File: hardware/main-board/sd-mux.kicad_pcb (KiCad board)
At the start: 2 copper layers, 75.4 x 114 mm, 91 parts, among them J1 USDCARD, P1 USB_OTG, P10 BARREL_JACK, P2 61400416021, P3 61400416021, P4 CONN_01X06, P5 BARREL_JACK, P6 IDC_02X04, P7 IDC_02X04, P8 USB_OTG, P9 USB_A, Q1 IRF7606PBF, Q2 IRF7606PBF, Q3 IRF7606PBF, Q4 IRF7606PBF, Q5 2N7002, Q6 2N7002, Q7 IRF7606PBF, Q8 IRF7606PBF, U1 TS3USB30EDGSR, U2 FT245RL, U3 TUSB4041IPAPR, U4 74AHC1G14, U5 TLV73333, U6 TLV73311, U7 74AHC1G14, U8 TS3A27518E, Y1 24MHz

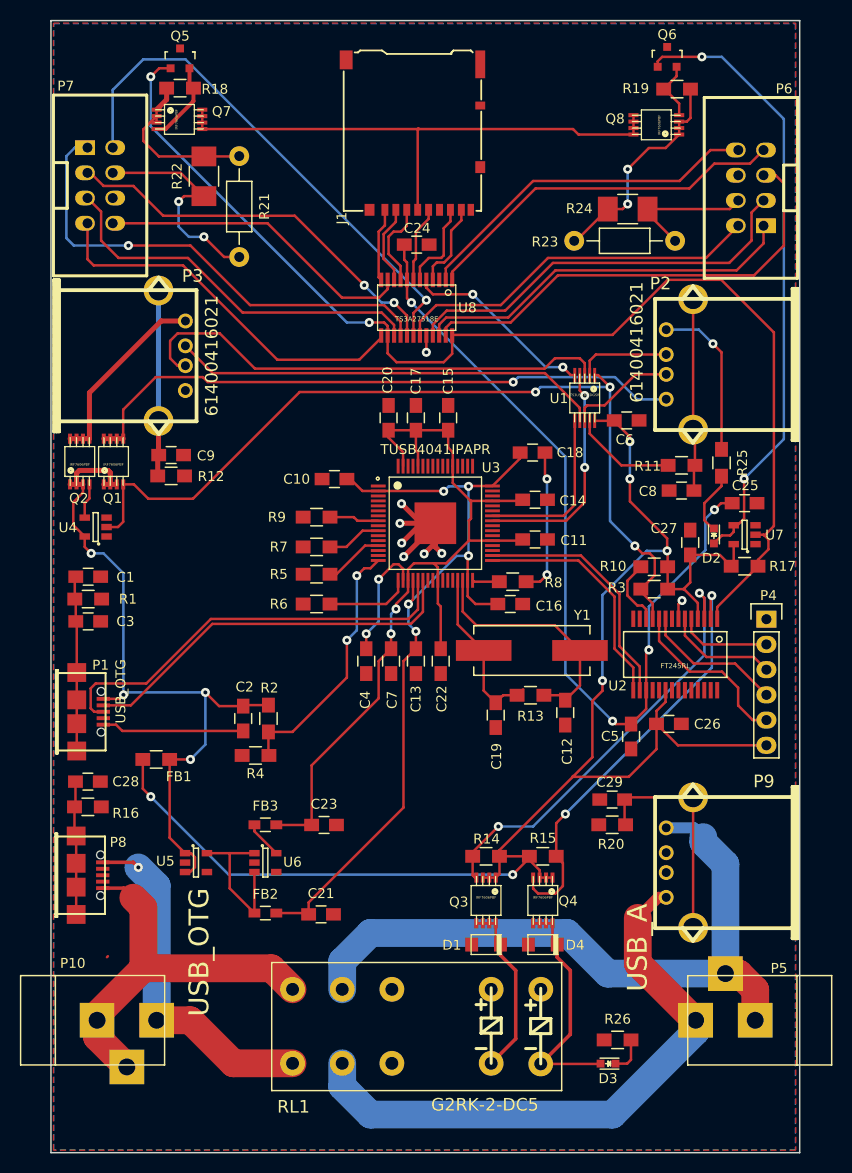
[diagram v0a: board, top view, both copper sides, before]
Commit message: Update BOM and layout labels
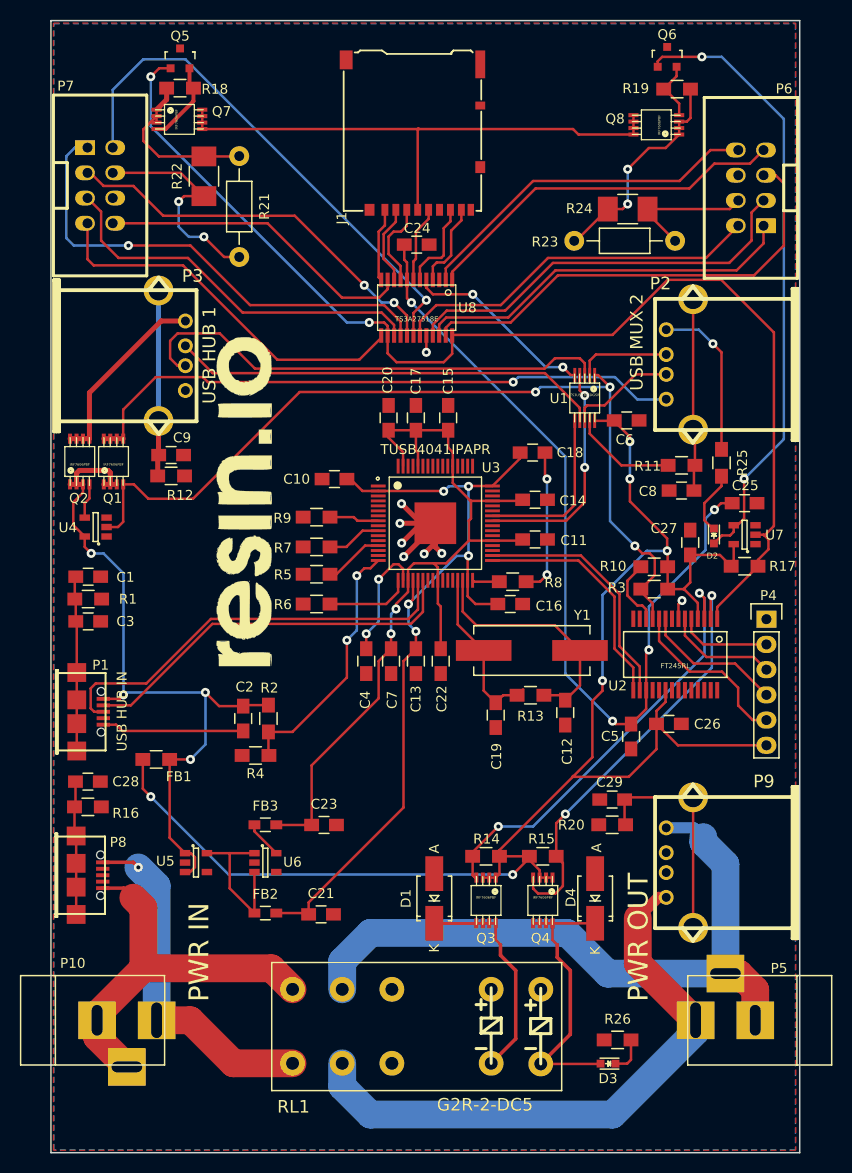
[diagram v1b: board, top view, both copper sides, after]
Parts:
- added G***: LOGO, footprints:logo, F.Cu at (137.7, 82.0)
- D1, D4: value ES1AL -> ES1A-LTP; footprint footprints:do219ab -> Diodes_SMD:SMA_Handsoldering
- P1: value USB_OTG -> USB HUB IN
- P2: value 61400416021 -> USB MUX 2
- P3: value 61400416021 -> USB HUB 1
- P8: value USB_OTG -> PWR IN
- P9: value USB_A -> PWR OUT
- RL1: value G2RK-2-DC5 -> G2R-2-DC5
- moved D4 7.03 mm to (173.0, 122.0), turned to 90 degrees
- moved D1 6.98 mm to (156.8, 122.0), turned to 90 degrees
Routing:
- net Net-(D1-Pad1): track 17.9 -> 26.2 mm
- net Net-(D3-Pad2): track 24.2 -> 28.5 mm

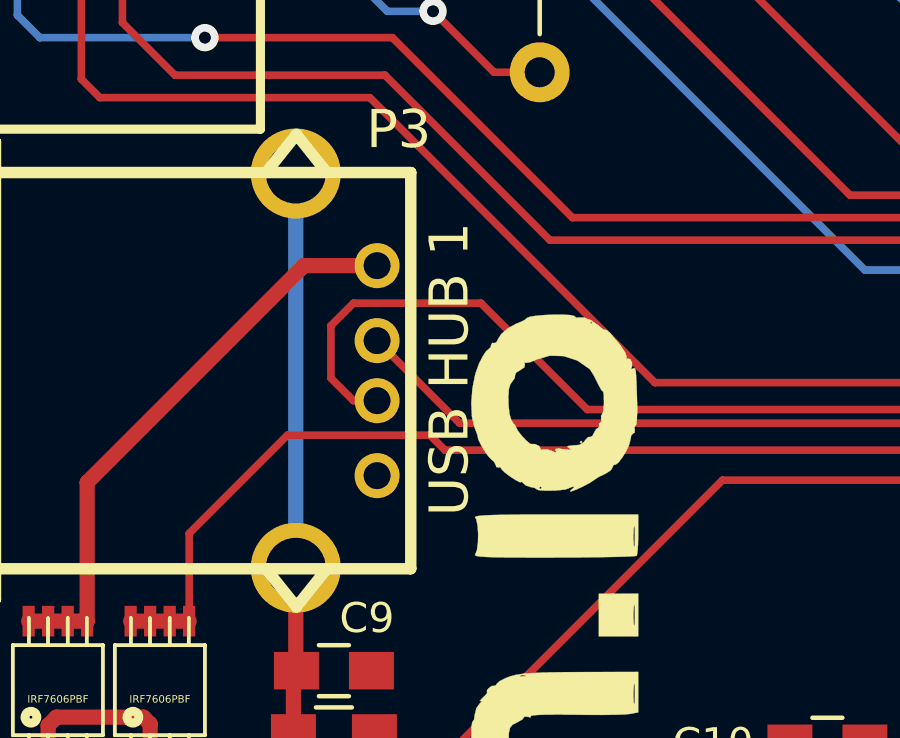
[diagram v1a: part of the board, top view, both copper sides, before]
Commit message: Add fabrication files for second iteration
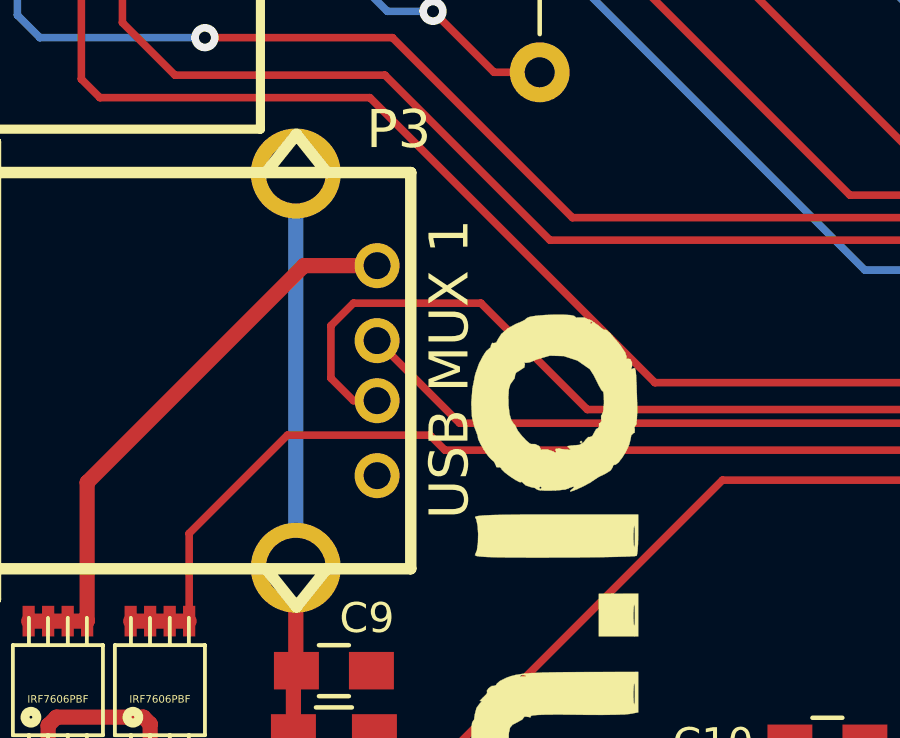
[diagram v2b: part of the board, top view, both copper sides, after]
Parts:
- P3: value USB HUB 1 -> USB MUX 1
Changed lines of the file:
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@@
       (effects (font (thickness 0.3048)))
     )
-    (fp_text value "USB HUB 1" (at -0.05 -8.4 270) (layer F.SilkS)
+    (fp_text value "USB MUX 1" (at -0.05 -8.4 270) (layer F.SilkS)
       (effects (font (size 1.3 1.3) (thickness 0.3048)))
     )
